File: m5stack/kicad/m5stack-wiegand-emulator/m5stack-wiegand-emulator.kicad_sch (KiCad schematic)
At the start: 42 parts, among them J1 2x15 socket header, J2 2x15 pin header, J3 1x5 female, T1 TestPoint, T2 TestPoint, T3 TestPoint, T4 TestPoint, U1 RP2040, U2 ISOW7841, U3 SN74LVC2G126-EP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

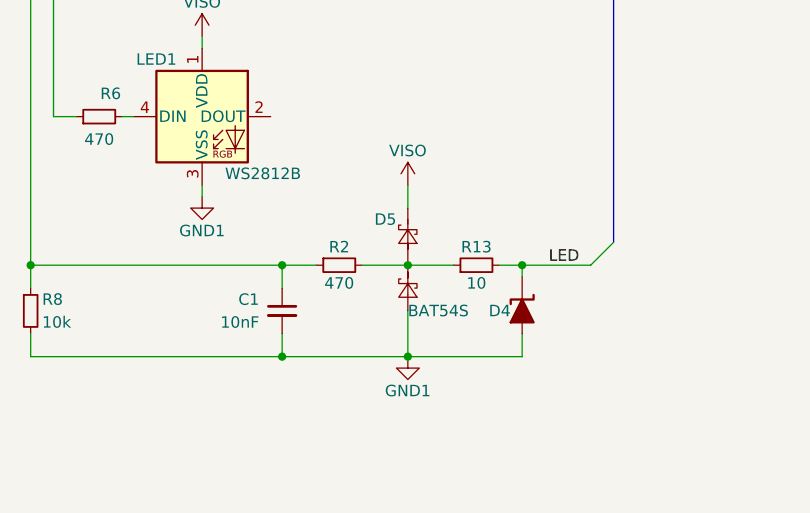
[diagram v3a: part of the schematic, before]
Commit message: M5: recalculated LED input resistance
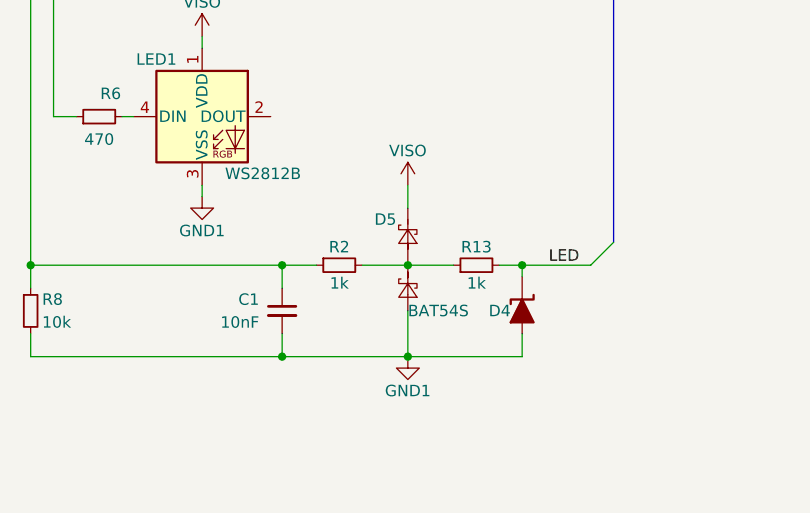
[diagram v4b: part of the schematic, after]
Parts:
- R13: value 10 -> 1k
- R2: value 470 -> 1k
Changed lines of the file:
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@@
       (effects (font (size 1.27 1.27)) (justify bottom))
     )
-    (property "Value" "470" (at 226.06 139.7 90)
+    (property "Value" "1k" (at 226.06 139.7 90)
       (effects (font (size 1.27 1.27)) (justify top))
     )
@@
       (effects (font (size 1.27 1.27)) (justify top))
     )
-    (property "Value" "10" (at 241.3 139.7 90)
+    (property "Value" "1k" (at 241.3 139.7 90)
       (effects (font (size 1.27 1.27)) (justify bottom))
     )

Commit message: M5: routing PWR
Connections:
- net GND: now also R1.5 (R4.2); no longer R1.2 (R1.2)
- net at U1.16 (GP7), U2.4 (INB): now also R1.8 (R6.2); no longer R1.4 (R3.2)
- net at U1.17 (GP6), U2.3 (INA): now also R1.9 (R7.2); no longer R1.5 (R4.2)
- net at JP6.2 (B), U1.19 (GP4): now also R1.2 (R1.2); no longer R1.8 (R6.2)
- net at U1.15 (GP8), U2.5 (INC): now also R1.7 (R5.2); no longer R1.3 (R2.2)
- net at JP4.2 (B), U1.23 (GP0): now also R1.4 (R3.2); no longer R1.10 (R8.2)
- net at JP7.2 (B), U1.18 (GP5): now also R1.10 (R8.2); no longer R1.7 (R5.2)
- net at JP5.2 (B), U1.22 (GP1): now also R1.3 (R2.2); no longer R1.9 (R7.2)
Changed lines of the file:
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@@
     (effects (font (size 1.27 1.27)) (justify left bottom))
   )
-  (symbol (lib_id "uhppoted:EXB-D10C103J_Split") (at 157.48 76.2 0) (unit 3)
+  (symbol (lib_id "uhppoted:EXB-D10C103J_Split") (at 157.48 76.2 0) (unit 6)
     (in_bom yes) (on_board yes) (dnp no)
     (property "Reference" "R1" (at 158.75 74.93 0)
@@
       (project "m5stack-wiegand-emulator"
         (path "/591217c3-ab1f-4851-a185-c0f7ee9f3d97"
-          (reference "R1") (unit 3)
+          (reference "R1") (unit 6)
         )
       )
@@
     )
   )
-  (symbol (lib_id "uhppoted:EXB-D10C103J_Split") (at 163.83 76.2 0) (unit 4)
+  (symbol (lib_id "uhppoted:EXB-D10C103J_Split") (at 163.83 76.2 0) (unit 7)
     (in_bom yes) (on_board yes) (dnp no)
     (property "Reference" "R1" (at 165.1 74.93 0)
@@
       (project "m5stack-wiegand-emulator"
         (path "/591217c3-ab1f-4851-a185-c0f7ee9f3d97"
-          (reference "R1") (unit 4)
+          (reference "R1") (unit 7)
         )
       )
@@
     )
   )
-  (symbol (lib_id "uhppoted:EXB-D10C103J_Split") (at 26.67 153.67 0) (unit 1)
+  (symbol (lib_id "uhppoted:EXB-D10C103J_Split") (at 26.67 153.67 0) (unit 4)
     (in_bom yes) (on_board yes) (dnp no)
     (property "Reference" "R1" (at 27.94 152.4 0)
@@
       (project "m5stack-wiegand-emulator"
         (path "/591217c3-ab1f-4851-a185-c0f7ee9f3d97"
-          (reference "R1") (unit 1)
+          (reference "R1") (unit 4)
         )
       )
@@
     )
   )
-  (symbol (lib_id "uhppoted:EXB-D10C103J_Split") (at 106.68 78.74 0) (unit 6)
+  (symbol (lib_id "uhppoted:EXB-D10C103J_Split") (at 106.68 78.74 0) (unit 1)
     (in_bom yes) (on_board yes) (dnp no)
     (property "Reference" "R1" (at 107.95 77.47 0)
@@
       (project "m5stack-wiegand-emulator"
         (path "/591217c3-ab1f-4851-a185-c0f7ee9f3d97"
-          (reference "R1") (unit 6)
+          (reference "R1") (unit 1)
         )
       )
@@
     )
   )
-  (symbol (lib_id "uhppoted:EXB-D10C103J_Split") (at 151.13 76.2 0) (unit 2)
+  (symbol (lib_id "uhppoted:EXB-D10C103J_Split") (at 151.13 76.2 0) (unit 5)
     (in_bom yes) (on_board yes) (dnp no)
     (property "Reference" "R1" (at 152.4 74.93 0)
@@
       (project "m5stack-wiegand-emulator"
         (path "/591217c3-ab1f-4851-a185-c0f7ee9f3d97"
-          (reference "R1") (unit 2)
+          (reference "R1") (unit 5)
         )
       )
@@
     )
   )
-  (symbol (lib_id "uhppoted:EXB-D10C103J_Split") (at 93.98 78.74 0) (unit 8)
+  (symbol (lib_id "uhppoted:EXB-D10C103J_Split") (at 93.98 78.74 0) (unit 3)
     (in_bom yes) (on_board yes) (dnp no)
     (property "Reference" "R1" (at 95.25 77.47 0)
@@
       (project "m5stack-wiegand-emulator"
         (path "/591217c3-ab1f-4851-a185-c0f7ee9f3d97"
-          (reference "R1") (unit 8)
+          (reference "R1") (unit 3)
         )
       )
@@
     )
   )
-  (symbol (lib_id "uhppoted:EXB-D10C103J_Split") (at 100.33 78.74 0) (unit 7)
+  (symbol (lib_id "uhppoted:EXB-D10C103J_Split") (at 100.33 78.74 0) (unit 2)
     (in_bom yes) (on_board yes) (dnp no)
     (property "Reference" "R1" (at 101.6 77.47 0)
@@
       (project "m5stack-wiegand-emulator"
         (path "/591217c3-ab1f-4851-a185-c0f7ee9f3d97"
-          (reference "R1") (unit 7)
+          (reference "R1") (unit 2)
         )
       )
@@
     )
   )
-  (symbol (lib_id "uhppoted:EXB-D10C103J_Split") (at 113.03 78.74 0) (unit 5)
+  (symbol (lib_id "uhppoted:EXB-D10C103J_Split") (at 113.03 78.74 0) (unit 8)
     (in_bom yes) (on_board yes) (dnp no)
     (property "Reference" "R1" (at 114.3 77.47 0)
@@
       (project "m5stack-wiegand-emulator"
         (path "/591217c3-ab1f-4851-a185-c0f7ee9f3d97"
-          (reference "R1") (unit 5)
-        )
-      )
+          (reference "R1") (unit 8)
+        )
+      )

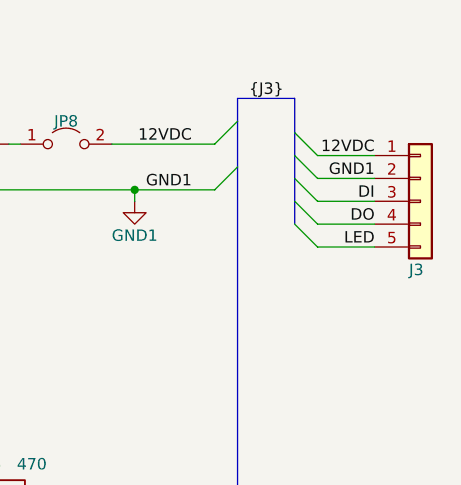
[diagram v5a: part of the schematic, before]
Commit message: M5: PCB routed and DRC'd
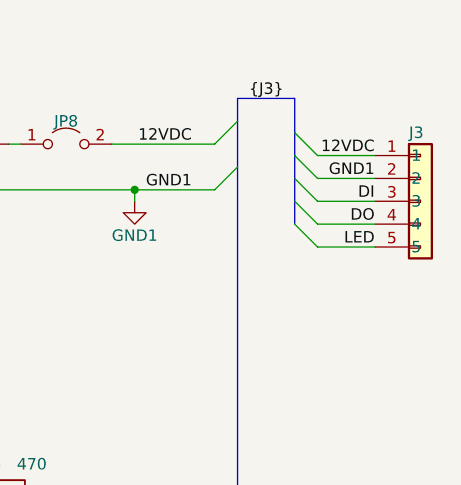
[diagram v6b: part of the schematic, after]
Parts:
- J3: footprint Connector_Molex:Molex_PicoBlade_53261-0571_1x05-1MP_P1.25mm_Horizontal -> uhppoted:Molex 532610571; symbol uhppoted:Molex_PicoBlade_1x05 -> uhppoted:Molex 532610571
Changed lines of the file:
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@@
     )
   )
-  (symbol (lib_id "uhppoted:Molex_PicoBlade_1x05") (at 276.86 41.91 0) (unit 1)
+  (symbol (lib_id "uhppoted:Molex 532610571") (at 270.51 36.83 0) (unit 1)
     (in_bom yes) (on_board yes) (dnp no)
-    (property "Reference" "J3" (at 275.59 49.53 0)
+    (property "Reference" "J3" (at 275.59 34.29 0)
       (effects (font (size 1.27 1.27)) (justify left))
     )
-    (property "Value" "1x5 female" (at 279.4 43.18 0)
+    (property "Value" "1x5 female" (at 273.05 38.1 0)
       (effects (font (size 1.27 1.27)) (justify left) hide)
     )
-    (property "Footprint" "Connector_Molex:Molex_PicoBlade_53261-0571_1x05-1MP_P1.25mm_Horizontal" (at 276.86 41.91 0)
-      (effects (font (size 1.27 1.27)) hide)
+    (property "Footprint" "uhppoted:Molex 532610571" (at 292.1 53.34 0)
+      (effects (font (size 1.27 1.27) italic) hide)
     )
-    (property "Datasheet" "~" (at 276.86 41.91 0)
-      (effects (font (size 1.27 1.27)) hide)
+    (property "Datasheet" "https://www.molex.com/en-us/products/part-detail/532610571" (at 311.15 55.88 0)
+      (effects (font (size 1.27 1.27) italic) hide)
     )
     (pin "4")
@@
     (pin "5")
     (pin "1")
-    (pin "MP")
+    (pin "MP1")
+    (pin "MP2")
     (instances
       (project "m5stack-wiegand-emulator"

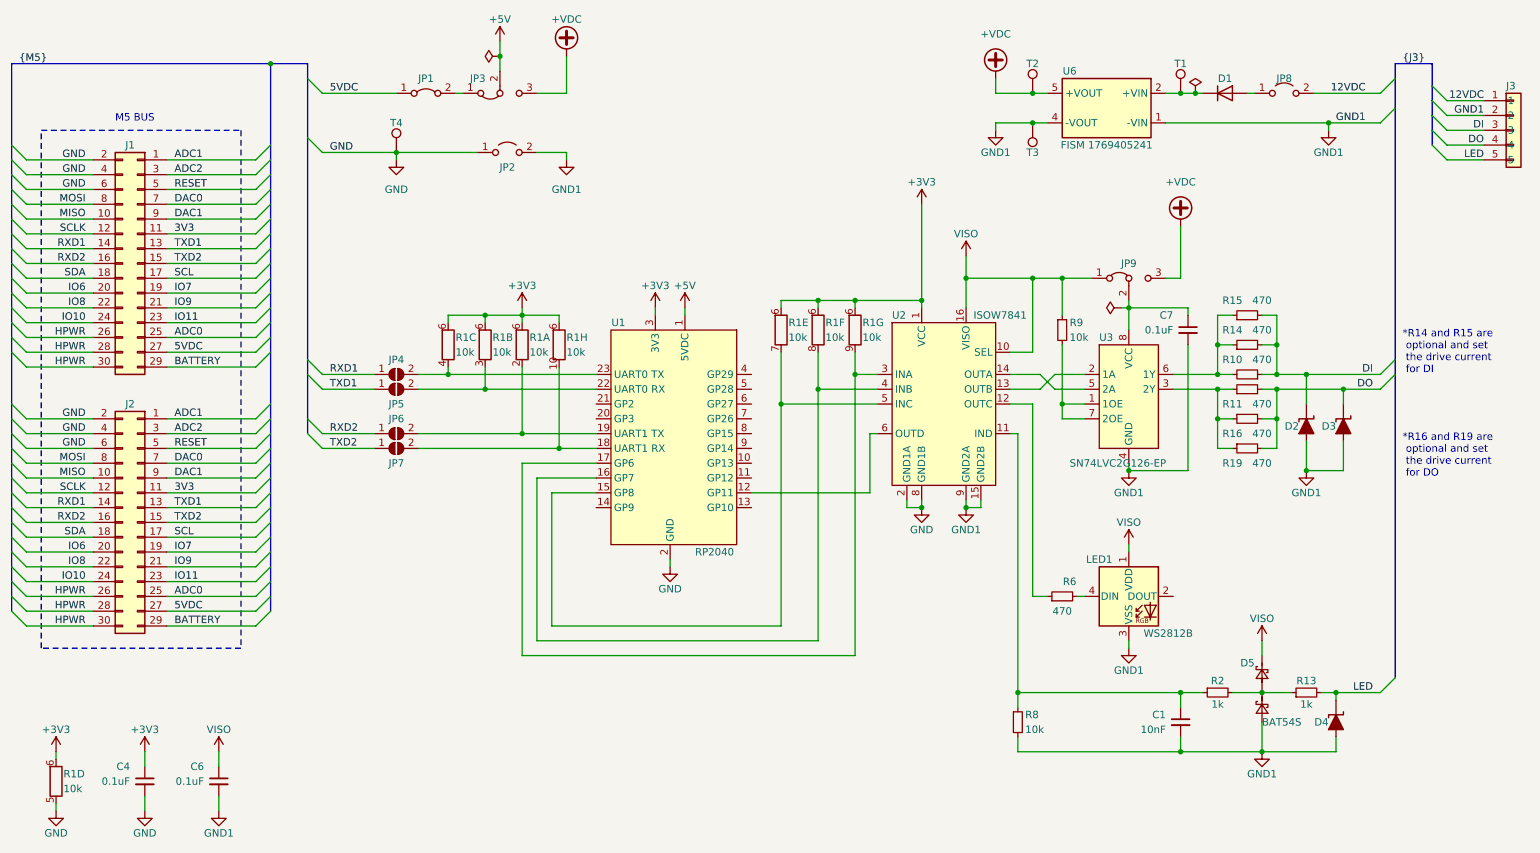
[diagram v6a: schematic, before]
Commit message: M5: replaced J1+J2 with single THT connector
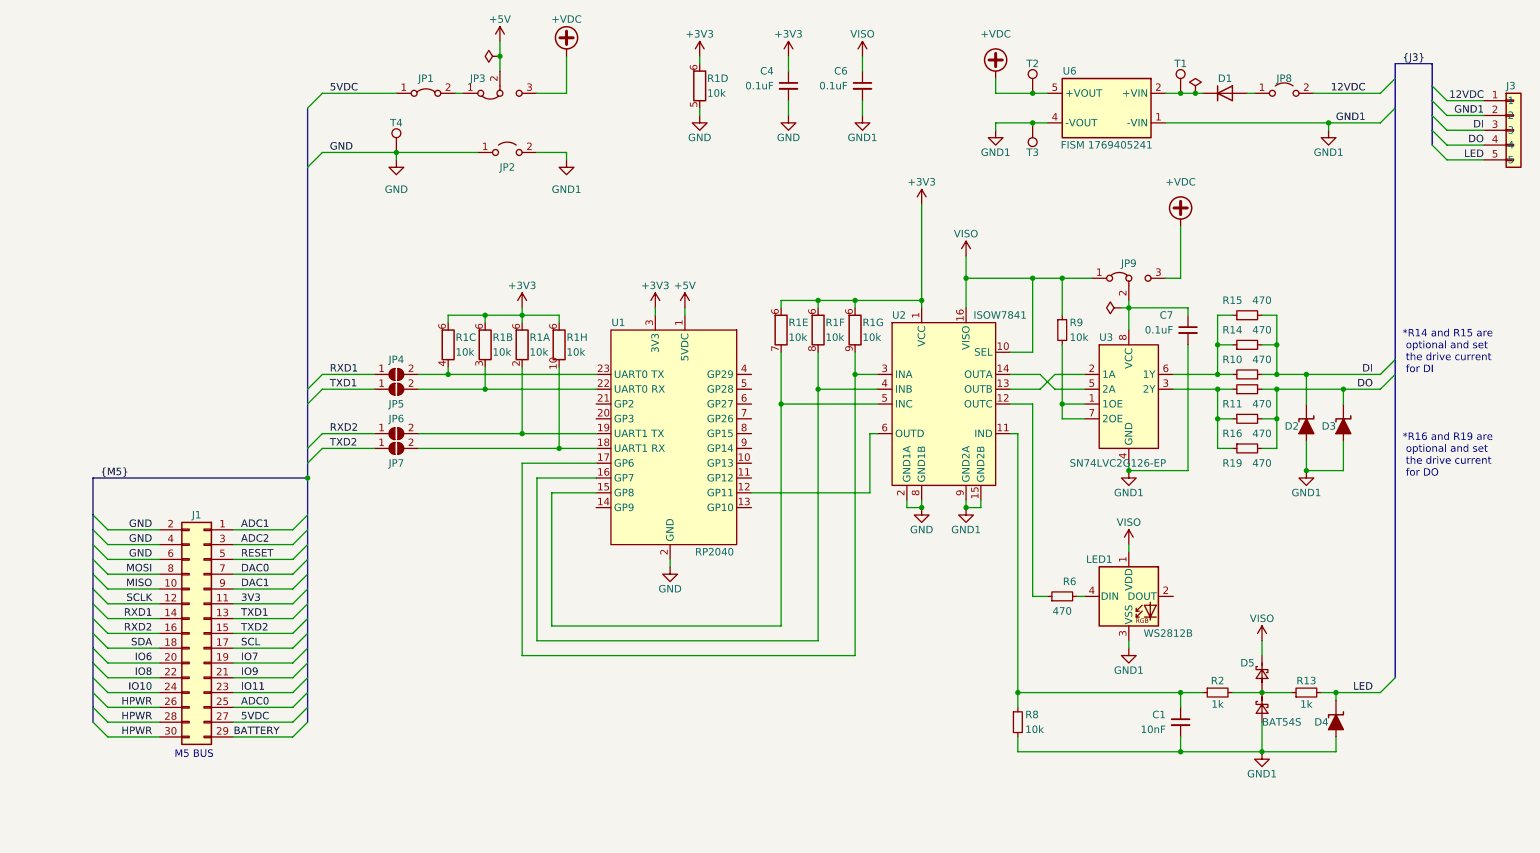
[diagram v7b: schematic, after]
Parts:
- removed J2: 2x15 pin header, Connector_PinHeader_2.54mm:PinHeader_2x15_P2.54mm_Vertical_SMD, symbol Connector_Generic:Conn_02x15_Odd_Even
- J1: footprint Connector_PinSocket_2.54mm:PinSocket_2x15_P2.54mm_Vertical_SMD -> uhppoted:M5 Bus connector
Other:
- moved on the sheet: C4, C6, J1, R1D

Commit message: M5: corrected ISOW7841 3D model
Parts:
- U2: footprint Package_SO:SOIC-16W_7.5x12.8mm_P1.27mm -> uhppoted:DWE0016A
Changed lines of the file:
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@@
       (effects (font (size 1.27 1.27)) (justify left))
     )
-    (property "Footprint" "Package_SO:SOIC-16W_7.5x12.8mm_P1.27mm" (at 179.07 119.38 0)
+    (property "Footprint" "uhppoted:DWE0016A" (at 179.07 119.38 0)
       (effects (font (size 1.27 1.27)) hide)
     )
